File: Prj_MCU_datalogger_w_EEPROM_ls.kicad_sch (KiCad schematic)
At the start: 25 parts, among them U1 24LC1025, U2 24LC1025, U3 ATMEGA328P-AU, U4 DS1337S_, Y1 16 MHz, Y2 32.768 kHz

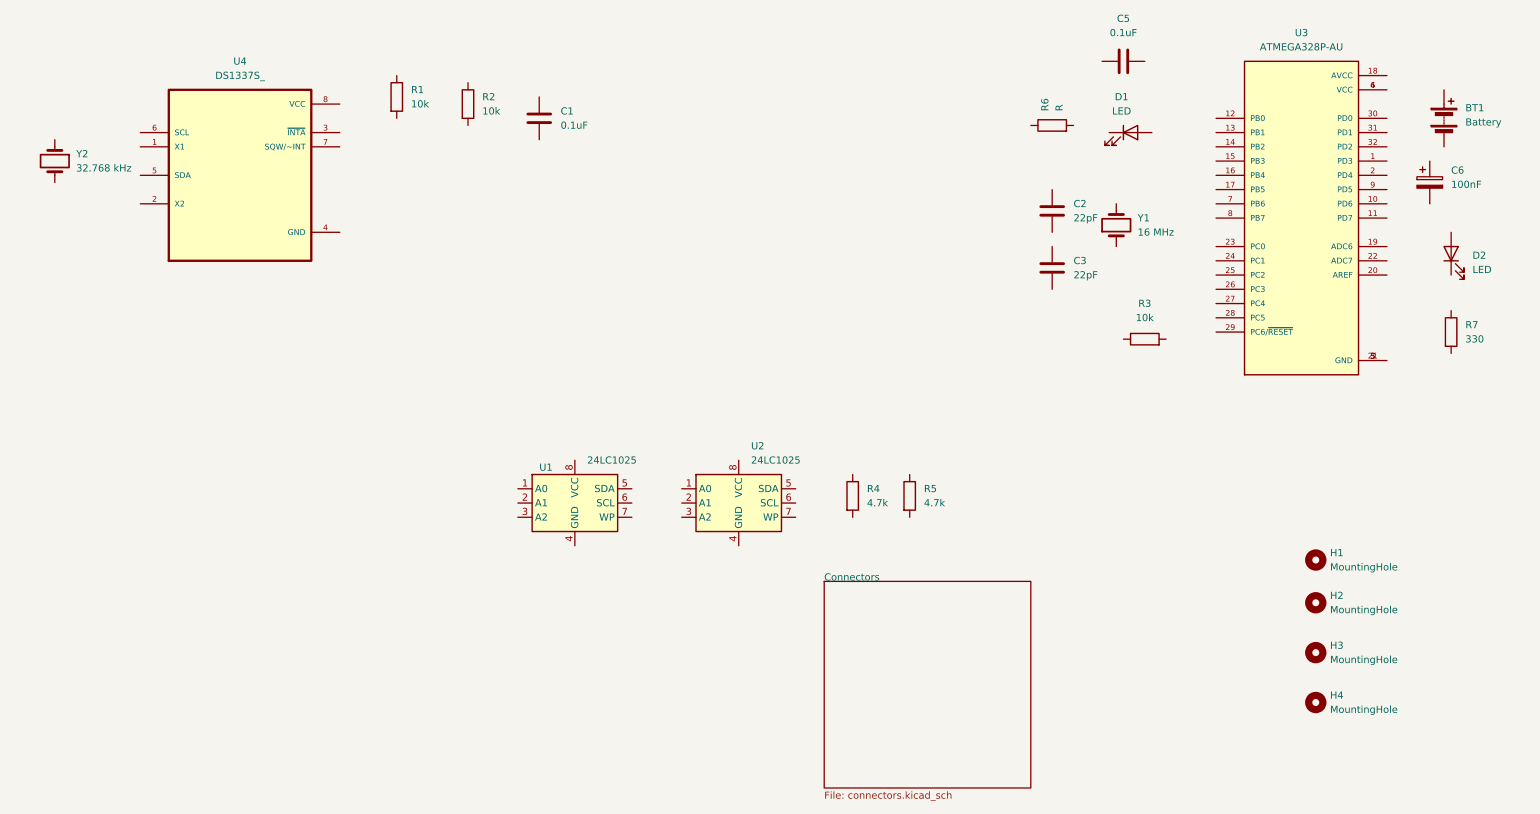
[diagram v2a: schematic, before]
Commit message: Completed wiring of main sheet.
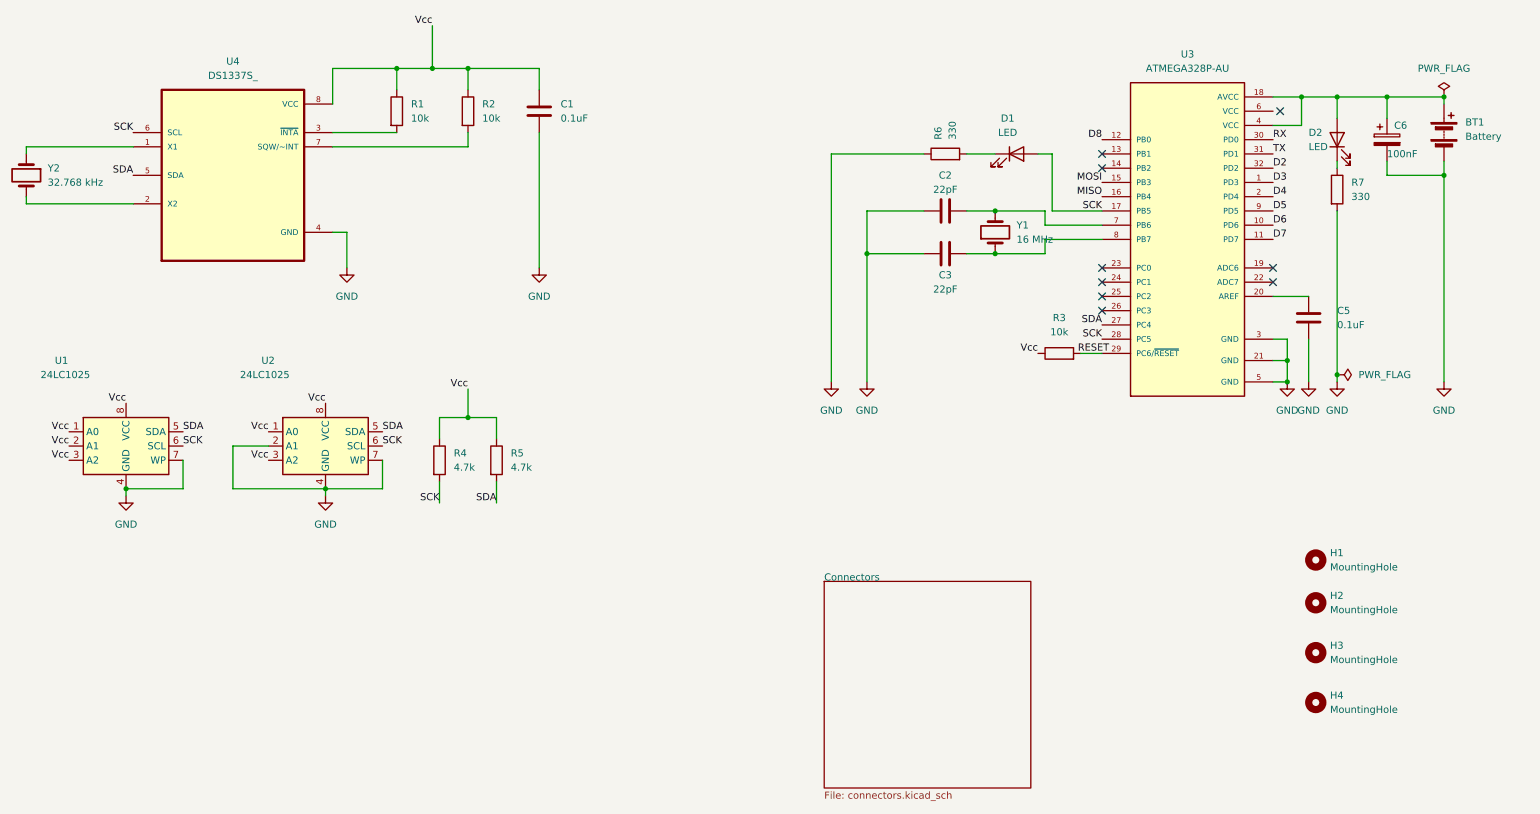
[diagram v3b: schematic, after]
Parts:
- R6: value R -> 330
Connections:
- net Vcc: now reaches R3.1
- net Vcc: now also C1.1, R1.1, R2.1, R4.1, R5.1, U1.1 (A0), U1.2 (A1), U1.3 (A2), U1.8 (VCC), U2.1 (A0), U2.3 (A2), U2.8 (VCC), U4.8 (VCC)
- net at R3.2: now also U3.29 (PC6/~{RESET})
- net at R2.2: now also U4.7 (SQW/~INT)
- net GND: now reaches U1.4 (GND)
- net GND: now also BT1.2 (-), C1.2, C2.1, C3.1, C5.1, C6.2, R6.1, R7.2, U1.7 (WP), U2.2 (A1), U2.4 (GND), U2.7 (WP), U3.21 (GND), U3.3 (GND), U3.5 (GND), U4.4 (GND)
- net SDA: now reaches U1.5 (SDA)
- net SDA: now also R5.2, U2.5 (SDA), U3.27 (PC4), U4.5 (SDA)
- net SCK: now reaches U1.6 (SCL)
- net SCK: now also D1.2 (A), R4.2, U2.6 (SCL), U3.17 (PB5), U3.28 (PC5), U4.6 (SCL)
- net at R1.2: now also U4.3 (~{INTA})
- net at R7.1: now also D2.1 (K)
- net at D1.1 (K): now also R6.2
- net D3: now reaches U3.1 (PD3)
- net D6: now reaches U3.10 (PD6)
- net D7: now reaches U3.11 (PD7)
- net D8: now reaches U3.12 (PB0)
- net MOSI: now reaches U3.15 (PB3)
- net MISO: now reaches U3.16 (PB4)
- net at U3.18 (AVCC): now also BT1.1 (+), C6.1, D2.2 (A), U3.4 (VCC)
- net D4: now reaches U3.2 (PD4)
- net at U3.20 (AREF): now also C5.2
- net RX: now reaches U3.30 (PD0)
- net TX: now reaches U3.31 (PD1)
- net D2: now reaches U3.32 (PD2)
- net at U3.6 (VCC): no longer U3.4 (VCC)
- net at U3.7 (PB6): now also C2.2, Y1.2
- net at U3.8 (PB7): now also C3.2, Y1.1
- net D5: now reaches U3.9 (PD5)
- net at U4.1 (X1): now also Y2.1
- net at U4.2 (X2): now also Y2.2
- no-connect marks 0 -> 9
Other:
- moved on the sheet: BT1, C1, C2, C3, C5, C6, D1, D2, R1, R2, R3, R4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

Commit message: Completed wiring of secondary sheet.
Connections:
- net RESET: now also R3.2, U3.29 (PC6/~{RESET})
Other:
- sheet Connectors ports: added D2, D3, D4, D5, D6, D7, D8, GND, MISO, MOSI, RESET, RX, SCK, SDA, TX, Vcc; removed none
